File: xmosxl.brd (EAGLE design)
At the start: 130 x 85 mm, 1 part

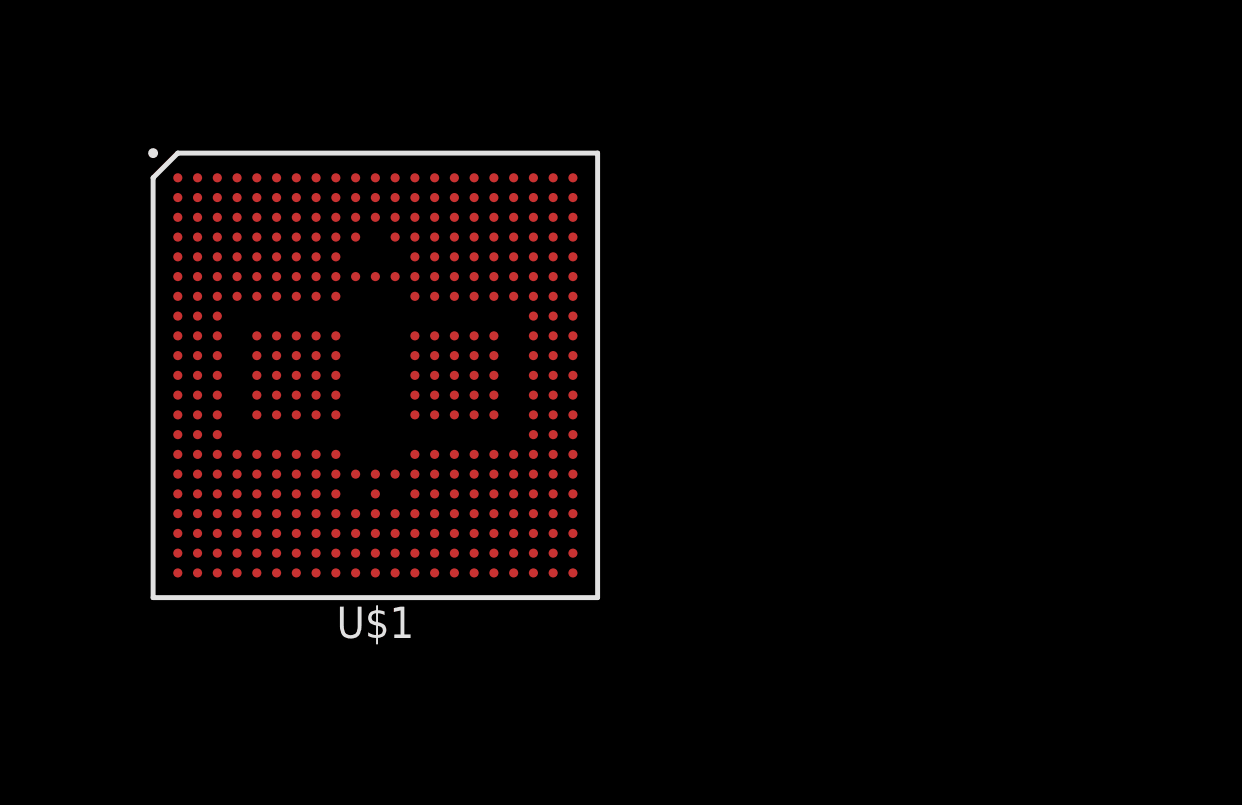
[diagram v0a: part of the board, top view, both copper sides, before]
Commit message: Just test the .gitignore for eagle files
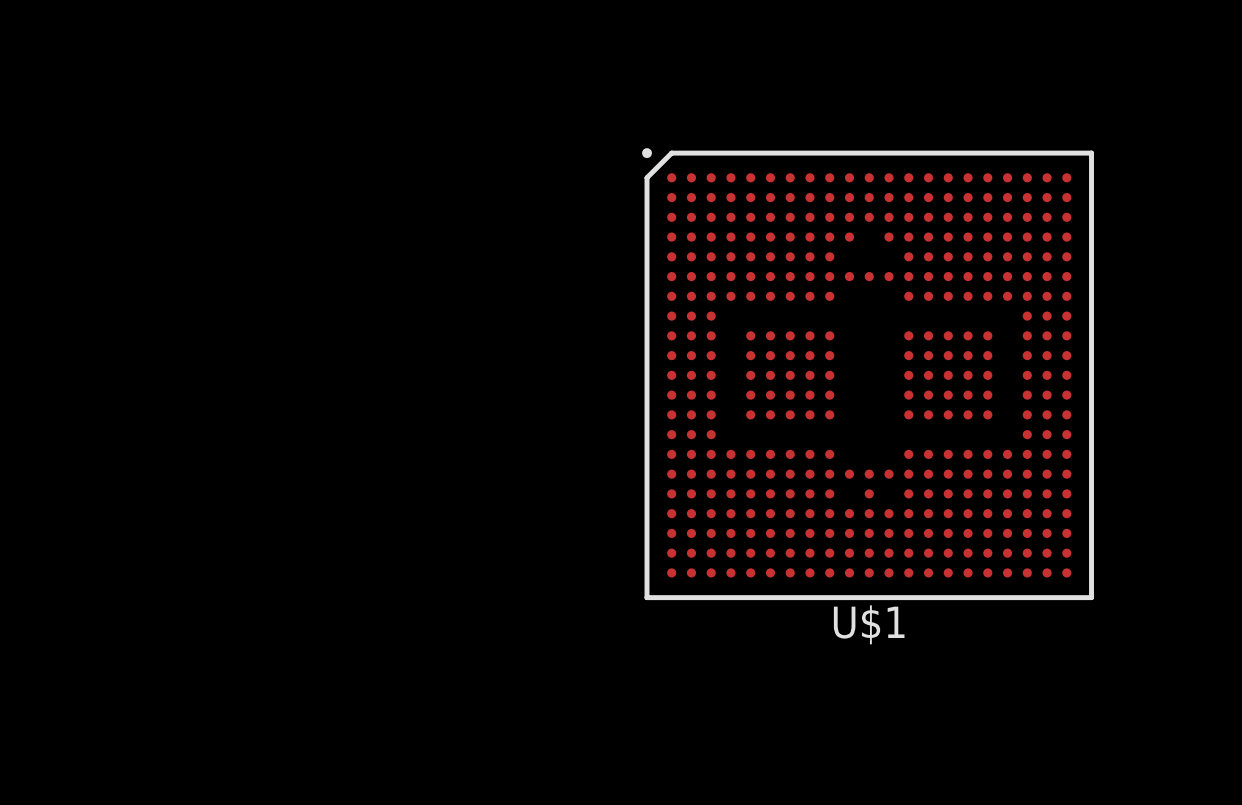
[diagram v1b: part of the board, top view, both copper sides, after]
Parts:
- moved U$1 20.0 mm to (50.0, 60.0)
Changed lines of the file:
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@@
 </autorouter>
 <elements>
-<element name="U$1" library="xmosxl" package="BGA374C80P21X21_1800X1800X136" value="XEF232" x="30" y="60" smashed="yes">
-<attribute name="NAME" x="30" y="50" size="1.27" layer="25" align="center"/>
-<attribute name="VALUE" x="30" y="70" size="1.27" layer="27" align="center"/>
+<element name="U$1" library="xmosxl" package="BGA374C80P21X21_1800X1800X136" value="XEF232" x="50" y="60" smashed="yes">
+<attribute name="NAME" x="50" y="50" size="1.27" layer="25" align="center"/>
+<attribute name="VALUE" x="50" y="70" size="1.27" layer="27" align="center"/>
 </element>
 </elements>

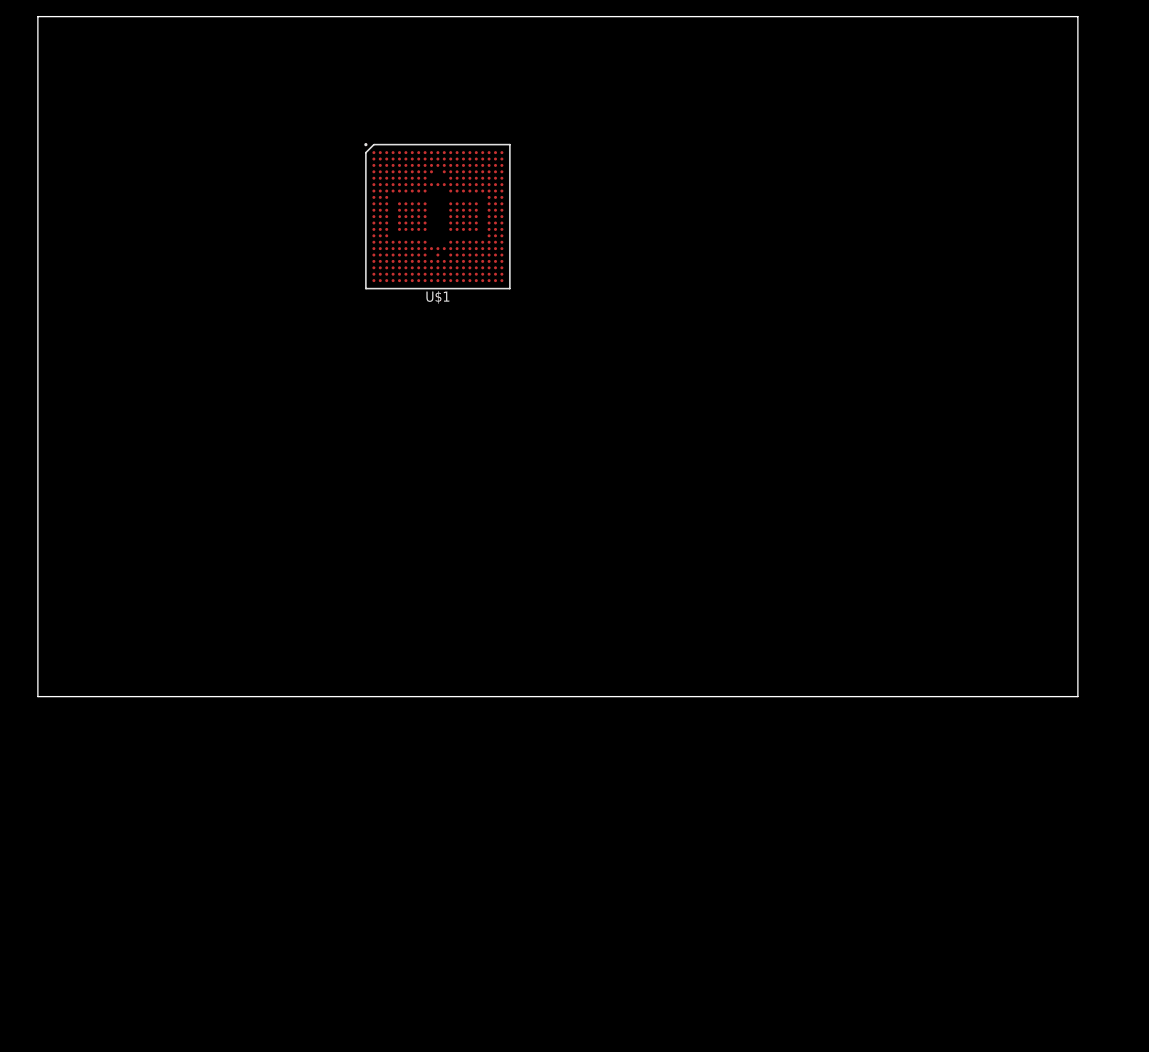
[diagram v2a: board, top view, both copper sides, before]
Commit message: Start to lay out the design. Add slots and holes to take up space, and start to populate the level converters / vregs
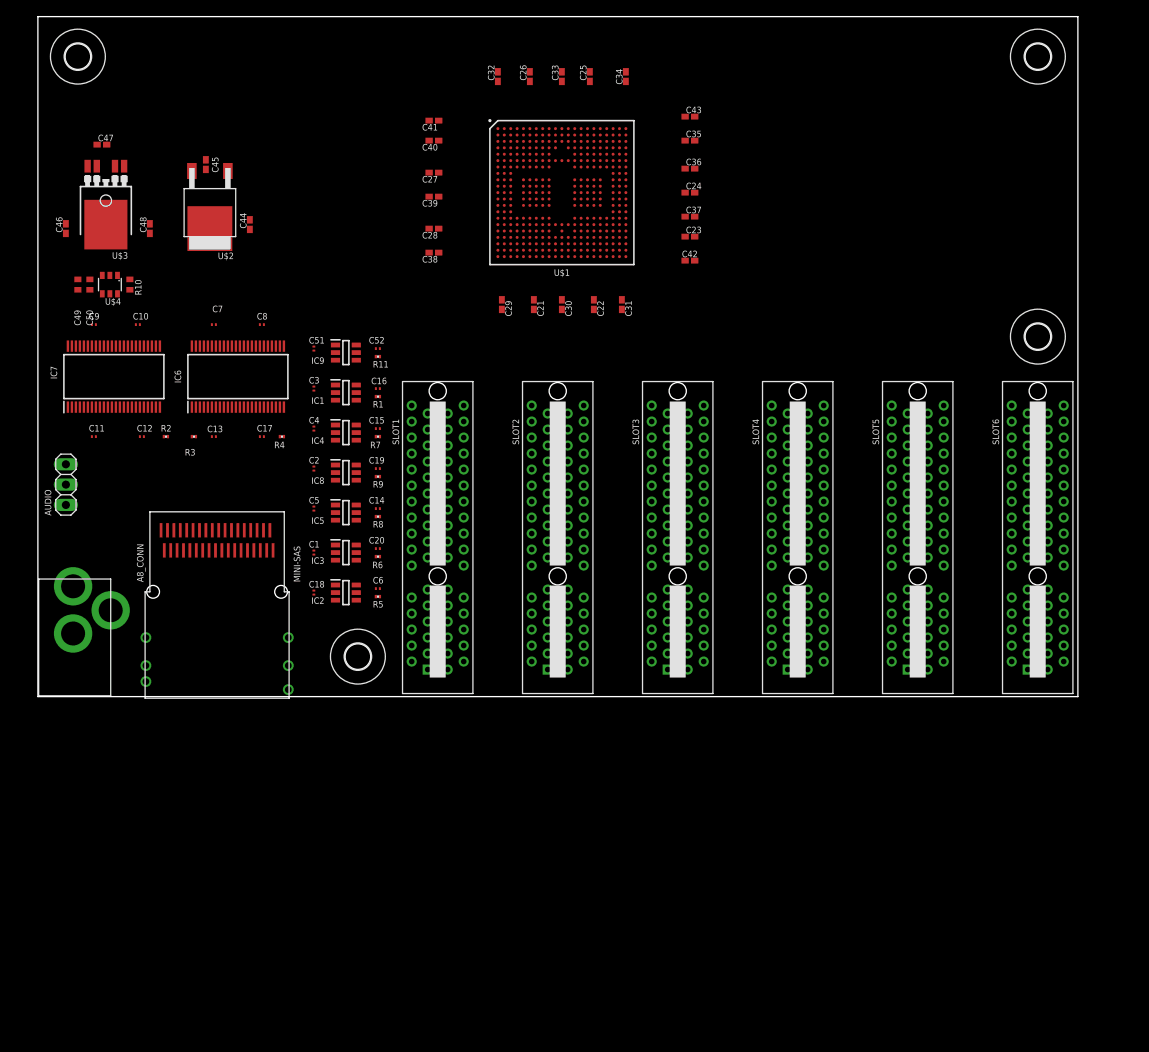
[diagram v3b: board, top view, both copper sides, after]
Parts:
- added A8_CONN: MINI-SAS, sjg-con:MINI-SAS
- added AUDIO: AUDIO, pinhead:1X03
- added C1, C10, C11, C12, C13, C14, C15, C16, C17, C18, C19, C2, C20, C3, C4, C5, C51, C52, C6, C7, C8, C9: 0.1uF, rcl:C0201
- added C21, C22, C23, C24, C25, C26, C27, C28, C29, C30, C31, C32, C33, C34, C35, C36, C37, C38, C39, C40, C43: 0.1uF, rcl:C0402K
- added C41, C42, C44, C45, C47: 10uF, rcl:C0402K
- added C46, C48: 1uF, rcl:C0402K
- added C49: 0.1uF, rcl:C0402
- added C50: 120pF, rcl:C0402
- added H1, H2, H3, H4: MOUNT-HOLE3.2, holes:3,2
- added IC1, IC2, IC3, IC4, IC5, IC8, IC9: 74LVC1T45W6-7, samacsys:SOT95P285X140-6N
- added IC6, IC7: 74ALVC164245DGG_11, samacsys:SOP50P810X120-48N
- added PJ-102AH: PJ-102AH, adafruit:PJ-102A
- added R1, R11, R2, R3, R4, R5, R6, R7, R8, R9: 10K, rcl:R0201
- added R10: 47K, rcl:R0402
- added SLOT1, SLOT2, SLOT3, SLOT4, SLOT5, SLOT6: PCIE_64, pcie:PCI-E_64
- added U$2: AP7363-330-13, sjg-power:TO252-3L
- added U$3: LD49300, sjg-power:TO252-51
- added U$4: TPS3808G33DBVR, sjg-power:SOT23-6
- moved U$1 15.8 mm to (65.5, 63.0)
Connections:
- new net !EXTSEL!: IC9.4
- new net !EXTSEL!_DIR: IC9.5, R11.2
- new net !HALT!: IC4.4
- new net !HALT!_DIR: IC4.5, R7.1
- new net !HI_EXTSEL!: A8_CONN.PB13, IC9.3
- new net !HI_HALT!: A8_CONN.PA14, IC4.3
- new net !HI_IRQ!: A8_CONN.PB14, IC3.3
- new net !HI_MPD!: A8_CONN.PA15, IC5.3
- new net !HI_REF!: A8_CONN.PB16, IC8.3
- new net !HI_RST!: A8_CONN.PA17, IC2.3
- new net !IRQ!: IC3.4
- new net !IRQ!_DIR: IC3.5, R6.1
- new net !MPD!: IC5.4
- new net !MPD!_DIR: IC5.5, R8.1
- new net !REF!: IC8.4
- new net !REF!_DIR: IC8.5, R9.1
- new net !RST!: IC2.4
- new net !RST!_DIR: IC2.5, R5.1
- new net +3V3: C10.1, C14.1, C15.1, C16.1, C19.1, C20.1, C21.1, C22.1, C23.1, C24.1, C25.1, C26.1, C27.1, C28.1, C41.1, C43.1, C45.1, C49.1, C52.1, C6.1, C7.1, C8.1, C9.1, IC1.6, IC2.6, IC3.6, IC4.6, IC5.6, IC6.31, IC6.42, IC7.31, IC7.42, IC8.6, IC9.6, R1.2, R10.2, R11.1, R5.2, R6.2, R7.2, R8.2, R9.2, U$1.A11, U$1.A16, U$1.A2, U$1.A20, U$1.A6, U$1.AA11, U$1.AA2, U$1.AA20, U$1.D7, U$1.E15, U$1.E7, U$1.F2, U$1.F20, U$1.L1, U$1.L21, U$1.T2, U$1.T20, U$1.U11, U$1.U15, U$1.U7, U$2.P$3, U$4.5, U$4.6
- new net +5V: C1.1, C11.1, C12.1, C13.1, C17.1, C18.1, C2.1, C3.1, C4.1, C44.1, C46.1, C48.1, C5.1, C51.1, IC1.1, IC2.1, IC3.1, IC4.1, IC5.1, IC6.18, IC6.7, IC7.18, IC7.7, IC8.1, IC9.1, PJ-102AH.TIP, U$2.P$1, U$3.2, U$3.5
- new net A0: IC7.47
- new net A1: IC7.46
- new net A10: IC7.33
- new net A11: IC7.32
- new net A12: IC7.30
- new net A13: IC7.29
- new net A14: IC7.27
- new net A15: IC7.26
- new net A2: IC7.44
- new net A3: IC7.43
- new net A4: IC7.41
- new net A5: IC7.40
- new net A6: IC7.38
- new net A7: IC7.37
- new net A8: IC7.36
- new net A9: IC7.35
- new net AUDIO_L: A8_CONN.PB18, AUDIO.3
- new net AUDIO_R: A8_CONN.PA18, AUDIO.1
- new net A_DIR: IC7.1, IC7.24, R2.1
- new net CLK: IC6.33
- new net CTRL_DIR: IC6.24, R4.1
- new net D0: IC6.47
- new net D1: IC6.46
- new net D2: IC6.44
- new net D3: IC6.43
- new net D4: IC6.41
- new net D5: IC6.40
- new net D6: IC6.38
- new net D7: IC6.37
- new net D_DIR: IC6.1, R3.1
- new net EN_1V0: R10.1, U$3.1, U$4.1
- new net GND: A8_CONN.SHIELD1, A8_CONN.SHIELD2, A8_CONN.SHIELD3, A8_CONN.SHIELD4, A8_CONN.SHIELD5, A8_CONN.SHIELD6, AUDIO.2, C1.2, C10.2, C11.2, C12.2, C13.2, C14.2, C15.2, C16.2, C17.2, C18.2, C19.2, C2.2, C20.2, C21.2, C22.2, C23.2, C24.2, C25.2, C26.2, C27.2, C28.2, C29.2, C3.2, C30.2, C31.2, C32.2, C33.2, C34.2, C35.2, C36.2, C37.2, C38.2, C39.2, C4.2, C40.2, C41.2, C42.2, C43.2, C44.2, C45.2, C46.2, C47.2, C48.2, C49.2, C5.2, C50.2, C51.2, C52.2, C6.2, C7.2, C8.2, C9.2, IC1.2, IC2.2, IC3.2, IC4.2, IC5.2, IC6.10, IC6.15, IC6.17, IC6.19, IC6.20, IC6.21, IC6.22, IC6.23, IC6.25, IC6.26, IC6.27, IC6.28, IC6.29, IC6.30, IC6.32, IC6.34, IC6.39, IC6.4, IC6.45, IC6.48, IC7.10, IC7.15, IC7.21, IC7.25, IC7.28, IC7.34, IC7.39, IC7.4, IC7.45, IC7.48, IC8.2, IC9.2, PJ-102AH.RING, R2.2, R3.2, R4.2, U$1.A1, U$1.A21, U$1.AA1, U$1.AA21, U$1.B11, U$1.C15, U$1.C7, U$1.D6, U$1.E16, U$1.E6, U$1.F19, U$1.F3, U$1.J13, U$1.J14, U$1.J15, U$1.J16, U$1.J17, U$1.J5, U$1.J6, U$1.J7, U$1.J8, U$1.J9, U$1.K13, U$1.K14, U$1.K15, U$1.K16, U$1.K17, U$1.K5, U$1.K6, U$1.K7, U$1.K8, U$1.K9, U$1.L13, U$1.L14, U$1.L15, U$1.L16, U$1.L17, U$1.L2, U$1.L20, U$1.L5, U$1.L6, U$1.L7, U$1.L8, U$1.L9, U$1.M13, U$1.M14, U$1.M15, U$1.M16, U$1.M17, U$1.M5, U$1.M6, U$1.M7, U$1.M8, U$1.M9, U$1.N13, U$1.N14, U$1.N15, U$1.N16, U$1.N17, U$1.N5, U$1.N6, U$1.N7, U$1.N8, U$1.N9, U$1.T11, U$1.T19, U$1.T3, U$1.U16, U$1.U6, U$1.W15, U$1.W7, U$1.Y11, U$2.P$2, U$3.TAB, U$4.2
- new net HI_A0: A8_CONN.PA1, IC7.2
- new net HI_A1: A8_CONN.PB1, IC7.3
- new net HI_A10: A8_CONN.PA6, IC7.16
- new net HI_A11: A8_CONN.PB6, IC7.17
- new net HI_A12: A8_CONN.PA7, IC7.19
- new net HI_A13: A8_CONN.PB7, IC7.20
- new net HI_A14: A8_CONN.PA8, IC7.22
- new net HI_A15: A8_CONN.PB8, IC7.23
- new net HI_A2: A8_CONN.PA2, IC7.5
- new net HI_A3: A8_CONN.PB2, IC7.6
- new net HI_A4: A8_CONN.PA3, IC7.8
- new net HI_A5: A8_CONN.PB3, IC7.9
- new net HI_A6: A8_CONN.PA4, IC7.11
- new net HI_A7: A8_CONN.PB4, IC7.12
- new net HI_A8: A8_CONN.PA5, IC7.13
- new net HI_A9: A8_CONN.PB5, IC7.14
- new net HI_CLK: A8_CONN.PA13, IC6.16
- new net HI_D0: A8_CONN.PA9, IC6.2
- new net HI_D1: A8_CONN.PB9, IC6.3
- new net HI_D2: A8_CONN.PA10, IC6.5
- new net HI_D3: A8_CONN.PB10, IC6.6
- new net HI_D4: A8_CONN.PA11, IC6.8
- new net HI_D5: A8_CONN.PB11, IC6.9
- new net HI_D6: A8_CONN.PA12, IC6.11
- new net HI_D7: A8_CONN.PB12, IC6.12
- new net HI_R/!W!: A8_CONN.PB17, IC1.3
- new net HI_RD4: A8_CONN.PB15, IC6.14
- new net HI_RD5: A8_CONN.PA16, IC6.13
- new net N$5: C50.1, U$4.4
- new net R/!W!: IC1.4
- new net R/!W!_DIR: IC1.5, R1.1
- new net RD4: IC6.35
- new net RD5: IC6.36
- new net VDD: C29.1, C30.1, C31.1, C32.1, C33.1, C34.1, C35.1, C36.1, C37.1, C38.1, C39.1, C40.1, C42.1, C47.1, U$1.C19, U$1.C3, U$1.E13, U$1.E14, U$1.E17, U$1.E18, U$1.E4, U$1.E5, U$1.E8, U$1.E9, U$1.F12, U$1.F13, U$1.F14, U$1.F15, U$1.F16, U$1.F17, U$1.F18, U$1.F4, U$1.F5, U$1.F6, U$1.F7, U$1.F8, U$1.F9, U$1.H19, U$1.H3, U$1.J19, U$1.J3, U$1.N19, U$1.N3, U$1.P19, U$1.P3, U$1.T10, U$1.T12, U$1.T13, U$1.T14, U$1.T16, U$1.T17, U$1.T18, U$1.T4, U$1.T5, U$1.T6, U$1.T8, U$1.T9, U$1.U13, U$1.U14, U$1.U17, U$1.U18, U$1.U4, U$1.U5, U$1.U9, U$3.4

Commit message: Add the SDRAM and start on JTAG
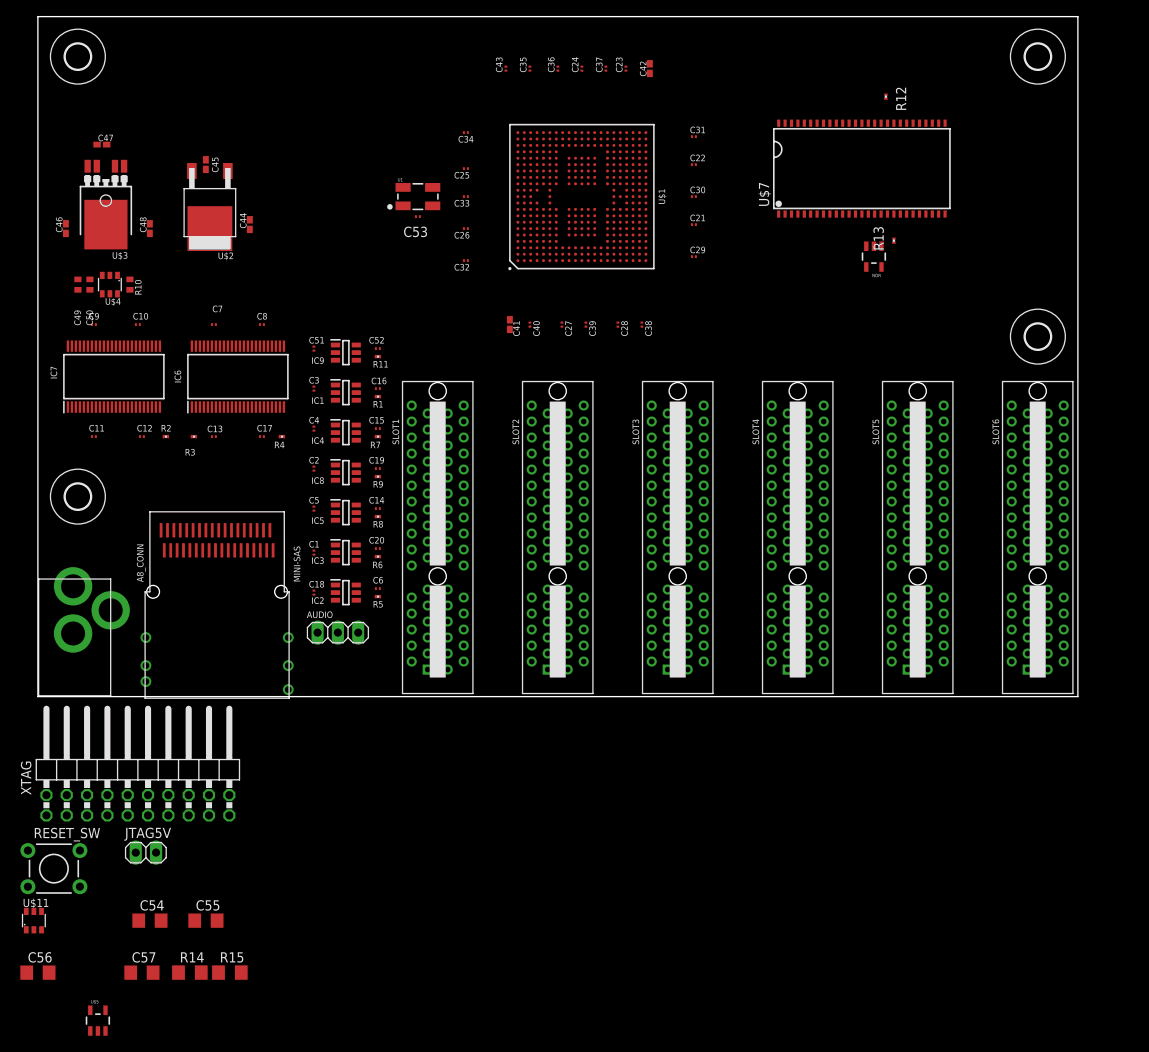
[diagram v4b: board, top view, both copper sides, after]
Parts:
- added C53: 10nF, rcl:C0201
- added C54, C55: 100nF, rcl:C1206
- added C56: 120pF, rcl:C1206
- added C57: 10nF, rcl:C1206
- added JTAG5V: PSU, pinhead:1X02
- added NOR: SN74LVC1G02, sjg-logic:SOT23-5
- added R12, R13: 10K, rcl:R0201
- added R14, R15: 47K, rcl:R1206
- added RESET_SW: MANUAL_RESET, SparkFun:TACTILE-PTH
- added U$11: TPS3808G09DBVR, sjg-power:SOT23-6
- added U$5: 74LVC1G07SE-7, sjg-logic:SOT23-5
- added U$7: W9852G6KH, sjg-sdram:TSOP54-400
- added U1: 24 MHz Osc. (F535L-24), SparkFun:CRYSTAL-OSC-SMD-5X3
- added XTAG: 1175-1618-ND, pinhead:2X10/90
- C21, C22, C23, C24, C25, C26, C27, C28, C29, C30, C31, C32, C33, C34, C35, C36, C37, C38, C39, C40, C43: device rcl:C0402K -> rcl:C0201
- moved H1 40.3 mm to (5.00, 25.0)
- moved AUDIO 38.7 mm to (37.5, 8.00), turned to 0 degrees
- moved C38 27.5 mm to (75.5, 46.5), turned to 270 degrees
- moved C41 27.2 mm to (59.0, 46.5), turned to 270 degrees
- moved C28 25.9 mm to (72.5, 46.5), turned to 270 degrees
- moved C40 25.9 mm to (61.5, 46.5), turned to 270 degrees
- moved C27 24.8 mm to (65.5, 46.5), turned to 270 degrees
- moved C39 24.8 mm to (68.5, 46.5), turned to 270 degrees
- moved C29 24.7 mm to (82.0, 55.0), turned to 0 degrees
- moved C42 24.5 mm to (76.5, 78.5), turned to 90 degrees
- moved C43 23.8 mm to (58.5, 78.5), turned to 90 degrees
- moved C32 23.3 mm to (53.5, 54.5), turned to 180 degrees
- moved C31 22.8 mm to (82.0, 70.0), turned to 0 degrees
- moved C23 22.5 mm to (73.5, 78.5), turned to 90 degrees
- moved C21 22.4 mm to (82.0, 59.0), turned to 0 degrees
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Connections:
- new net !RESET!: R15.1, U$11.1, U$5.4
- new net !SD_CAS!: NOR.1, U$1.Y18, U$7.17
- new net !SD_RAS!: U$1.Y13, U$7.18
- new net !SD_WE!: NOR.2, U$1.AA18, U$7.16
- new net JTAG_DN0: XTAG.14
- new net JTAG_DN1: XTAG.18
- new net JTAG_UP0: XTAG.10
- new net JTAG_UP1: XTAG.6
- new net N$1: R14.1, U$5.2, XTAG.15
- new net N$14: NOR.4, U$7.15, U$7.39
- new net N$15: R12.2, U$7.37
- new net N$17: R13.2, U$7.19
- new net N$2: U$1.A12, U1.3
- new net N$38: JTAG5V.2, XTAG.1
- new net N$4: C55.1, R15.2, U$11.6
- new net N$6: C56.1, U$11.4
- new net N$7: C54.1
- new net N$8: R14.2, U$5.5
- new net SD_ADQ0: U$1.AA13, U$7.2, U$7.23
- new net SD_ADQ1: U$1.W13, U$7.24, U$7.4
- new net SD_ADQ10: U$1.Y17, U$7.22, U$7.45
- new net SD_ADQ11: U$1.AA17, U$7.35, U$7.47
- new net SD_ADQ12: U$1.W21, U$7.36, U$7.48
- new net SD_ADQ13: U$1.V20, U$7.20, U$7.50
- new net SD_ADQ14: U$1.V21, U$7.21, U$7.51
- new net SD_ADQ15: U$1.U20, U$7.53
- new net SD_ADQ2: U$1.V13, U$7.25, U$7.5
- new net SD_ADQ3: U$1.W14, U$7.26, U$7.7
- new net SD_ADQ4: U$1.V14, U$7.29, U$7.8
- new net SD_ADQ5: U$1.Y14, U$7.10, U$7.30
- new net SD_ADQ6: U$1.AA14, U$7.11, U$7.31
- new net SD_ADQ7: U$1.Y12, U$7.13, U$7.32
- new net SD_ADQ8: U$1.V19, U$7.33, U$7.42
- new net SD_ADQ9: U$1.Y20, U$7.34, U$7.44
- new net SD_CLK: U$1.W12, U$7.38
- new net TCK: U$1.B13, XTAG.9
- new net TDI: U$1.A10, XTAG.5
- new net TDO: U$1.A13, XTAG.13
- new net TMS: U$1.D12, XTAG.7
- new net TRST_N: C57.2, RESET_SW.1, RESET_SW.2, U$11.3
- new net UART_RX: XTAG.19
- new net UART_TX: XTAG.17
- net +3V3: now also C53.2, NOR.5, R12.1, U$7.1, U$7.14, U$7.27, U$7.3, U$7.43, U$7.49, U$7.9, U1.4
- net +5V: now also JTAG5V.1
- net GND: now also C53.1, C54.2, C55.2, C56.2, C57.1, NOR.3, R13.1, RESET_SW.3, RESET_SW.4, U$11.2, U$5.3, U$7.12, U$7.28, U$7.41, U$7.46, U$7.52, U$7.54, U$7.6, U1.2, XTAG.12, XTAG.16, XTAG.20, XTAG.4, XTAG.8
- net VDD: now also U$11.5
